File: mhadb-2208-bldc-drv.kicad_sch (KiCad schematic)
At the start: 60 parts, among them J1 TC2030, J2 Conn_01x04_Pin, J3 Conn_01x04, M2 Motor_3_Phases, SW1 SW_Push, SW4 SW_Push, U1 AS5600-ASOT, U10 DRV8311H, U2 SN65HVD230, U3 STM32F103C8Tx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

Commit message: schem/pcb: add motor mounting holes
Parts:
- added H1, H2, H3: MountingHole_Pad, GLCS:MountingHole_3.2mm_M3_DIN965_Pad_Thin, symbol Mechanical:MountingHole_Pad
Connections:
- net EPAD: now also H1.1, H2.1, H3.1
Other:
- note added: "Motor mounting"

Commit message: schem/pcb: fix DRV8311 nsleep
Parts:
- removed C42: 100u, Capacitor_SMD:CP_Elec_6.3x7.7, symbol Device:C_Polarized
- added C16, C17, C18: 22u, Capacitor_SMD:C_1206_3216Metric, symbol Device:C
- added R7: 10k, Resistor_SMD:R_0402_1005Metric, symbol Device:R
- added R8: 5k1, Resistor_SMD:R_0402_1005Metric, symbol Device:R
- J3: footprint Connector_JST:JST_PH_S4B-PH-K_1x04_P2.00mm_Horizontal -> Connector_JST:JST_XH_B4B-XH-A_1x04_P2.50mm_Vertical; JLCPCB Part # C157926 -> C144395; Manufacturer Part Number S4B-PH-K-S(LF)(SN) -> B4B-XH-A(LF)(SN)
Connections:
- net +BATT: now also C16.1, C17.1, C18.1, R7.2
- net EPAD: now also U3.20 (PB2), C16.2, C17.2, C18.2, R8.2
- net +5V: no longer names the net of U10.24 (~{SLEEP})
- net +5V: now also R7.1, R8.1
- no-connect marks 18 -> 17
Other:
- moved on the sheet: C39

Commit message: pcb: initial rough placement
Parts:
- removed TP3, TP8, TP9: TestPoint, TestPoint:TestPoint_Pad_D2.0mm, symbol Connector:TestPoint
- M2: footprint Connector_PinHeader_2.54mm:PinHeader_1x03_P2.54mm_Vertical -> GLCS:Connector_Pad_1x03
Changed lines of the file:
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@@
 	)
 	(junction
-		(at 227.33 116.84)
-		(diameter 0)
-		(color 0 0 0 0)
-	)
-	(junction
 		(at 214.63 139.7)
 		(diameter 0)
@@
 	)
 	(junction
-		(at 233.68 99.06)
-		(diameter 0)
-		(color 0 0 0 0)
-	)
-	(junction
 		(at 217.17 99.06)
 		(diameter 0)
@@
 	(wire
 		(pts
-			(xy 222.25 116.84) (xy 227.33 116.84)
+			(xy 222.25 116.84) (xy 228.6 116.84)
 		)
 		(stroke
@@
 	(wire
 		(pts
-			(xy 229.87 99.06) (xy 233.68 99.06)
+			(xy 229.87 99.06) (xy 237.49 99.06)
 		)
 		(stroke
@@
 	(wire
 		(pts
-			(xy 227.33 116.84) (xy 228.6 116.84)
-		)
-		(stroke
-			(width 0)
-			(type default)
-		)
-	)
-	(wire
-		(pts
 			(xy 259.08 93.98) (xy 264.16 93.98)
 		)
@@
 	(wire
 		(pts
-			(xy 233.68 99.06) (xy 237.49 99.06)
-		)
-		(stroke
-			(width 0)
-			(type default)
-		)
-	)
-	(wire
-		(pts
 			(xy 217.17 99.06) (xy 218.44 99.06)
 		)
@@
 	)
 	(symbol
-		(lib_id "Connector:TestPoint")
-		(at 233.68 99.06 0)
-		(unit 1)
-		(exclude_from_sim no)
-		(in_bom no)
-		(on_board yes)
-		(dnp no)
-		(fields_autoplaced yes)
-		(property "Reference" "TP9"
-			(at 236.22 95.7579 0)
-			(effects
-				(font
-					(size 1.27 1.27)
-				)
-				(justify left)
-			)
-		)
-		(property "Value" "TestPoint"
-			(at 236.22 97.0279 0)
-			(effects
-				(font
-					(size 1.27 1.27)
-				)
-				(justify left)
-				(hide yes)
-			)
-		)
-		(property "Footprint" "TestPoint:TestPoint_Pad_D2.0mm"
-			(at 238.76 99.06 0)
-			(effects
-				(font
-					(size 1.27 1.27)
-				)
-				(hide yes)
-			)
-		)
-		(property "Datasheet" "~"
-			(at 238.76 99.06 0)
-			(effects
-				(font
-					(size 1.27 1.27)
-				)
-				(hide yes)
-			)
-		)
-		(property "Description" "test point"
-			(at 233.68 99.06 0)
-			(effects
-				(font
-					(size 1.27 1.27)
-				)
-				(hide yes)
-			)
-		)
-		(pin "1"
-		)
-		(instances
-			(project "mhadb-2208-bldc-drv"
-				(path "/68a41d17-d2bf-47b9-9455-3cb873e40984"
-					(reference "TP9")
-					(unit 1)
-				)
-			)
-		)
-	)
-	(symbol
 		(lib_id "power:GND")
 		(at 91.44 63.5 0)
@@
 			)
 		)
-		(property "Footprint" "Connector_PinHeader_2.54mm:PinHeader_1x03_P2.54mm_Vertical"
+		(property "Footprint" "GLCS:Connector_Pad_1x03"
 			(at 266.7 135.636 0)
 			(effects
@@
 	)
 	(symbol
-		(lib_id "Connector:TestPoint")
-		(at 227.33 116.84 0)
-		(unit 1)
-		(exclude_from_sim no)
-		(in_bom no)
-		(on_board yes)
-		(dnp no)
-		(property "Reference" "TP8"
-			(at 228.854 112.268 0)
-			(effects
-				(font
-					(size 1.27 1.27)
-				)
-				(justify left)
-			)
-		)
-		(property "Value" "TestPoint"
-			(at 229.87 114.8079 0)
-			(effects
-				(font
-					(size 1.27 1.27)
-				)
-				(justify left)
-				(hide yes)
-			)
-		)
-		(property "Footprint" "TestPoint:TestPoint_Pad_D2.0mm"
-			(at 232.41 116.84 0)
-			(effects
-				(font
-					(size 1.27 1.27)
-				)
-				(hide yes)
-			)
-		)
-		(property "Datasheet" "~"
-			(at 232.41 116.84 0)
-			(effects
-				(font
-					(size 1.27 1.27)
-				)
-				(hide yes)
-			)
-		)
-		(property "Description" "test point"
-			(at 227.33 116.84 0)
-			(effects
-				(font
-					(size 1.27 1.27)
-				)
-				(hide yes)
-			)
-		)
-		(pin "1"
-		)
-		(instances
-			(project "mhadb-2208-bldc-drv"
-				(path "/68a41d17-d2bf-47b9-9455-3cb873e40984"
-					(reference "TP8")
-					(unit 1)
-				)
-			)
-		)
-	)
-	(symbol
 		(lib_id "power:GND")
 		(at 257.81 151.13 0)
@@
 					(unit 1)
 				)
-			)
-		)
-	)
-	(symbol
-		(lib_id "Connector:TestPoint")
-		(at 222.25 147.32 90)
-		(unit 1)
-		(exclude_from_sim no)
-		(in_bom no)
-		(on_board yes)
-		(dnp no)
-		(property "Reference" "TP3"
-			(at 220.472 145.288 90)
-			(effects
-				(font
-					(size 1.27 1.27)
-				)
-				(justify left)
-			)
-		)
-		(property "Value" "TestPoint"
-			(at 220.2179 144.78 0)
-			(effects
-				(font
-					(size 1.27 1.27)
-				)
-				(justify left)
-				(hide yes)
-			)
-		)
-		(property "Footprint" "TestPoint:TestPoint_Pad_D2.0mm"
-			(at 222.25 142.24 0)
-			(effects
-				(font
-					(size 1.27 1.27)
-				)
-				(hide yes)
-			)
-		)
-		(property "Datasheet" "~"
-			(at 222.25 142.24 0)
-			(effects
-				(font
-					(size 1.27 1.27)
-				)
-				(hide yes)
-			)
-		)
-		(property "Description" "test point"
-			(at 222.25 147.32 0)
-			(effects
-				(font
-					(size 1.27 1.27)
-				)
-				(hide yes)
-			)
-		)
-		(pin "1"
-		)
-		(instances
-			(project "mhadb-2208-bldc-drv"
-				(path "/68a41d17-d2bf-47b9-9455-3cb873e40984"
-					(reference "TP3")
-					(unit 1)
-				)

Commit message: pcb: initial components placement
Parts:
- removed TP6: TestPoint, TestPoint:TestPoint_Pad_D2.0mm, symbol Connector:TestPoint
- added C19: 0u1, Capacitor_SMD:C_0402_1005Metric, symbol Device:C
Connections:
- net +3V3: now also C19.1
- net EPAD: now also C19.2
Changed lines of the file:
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@@
 	)
 	(junction
-		(at 254 74.93)
-		(diameter 0)
-		(color 0 0 0 0)
-	)
-	(junction
 		(at 91.44 52.07)
 		(diameter 0)
@@
 	)
 	(junction
-		(at 152.4 60.96)
-		(diameter 0)
-		(color 0 0 0 0)
-	)
-	(junction
 		(at 123.19 62.23)
 		(diameter 0)
@@
 	(wire
 		(pts
-			(xy 152.4 57.15) (xy 152.4 60.96)
+			(xy 152.4 57.15) (xy 152.4 64.77)
 		)
 		(stroke
@@
 	(wire
 		(pts
-			(xy 152.4 60.96) (xy 152.4 64.77)
-		)
-		(stroke
-			(width 0)
-			(type default)
-		)
-	)
-	(wire
-		(pts
 			(xy 81.28 181.61) (xy 81.28 182.88)
 		)
@@
 	(wire
 		(pts
-			(xy 255.27 74.93) (xy 254 74.93)
-		)
-		(stroke
-			(width 0)
-			(type default)
-		)
-	)
-	(wire
-		(pts
 			(xy 139.7 64.77) (xy 139.7 66.04)
 		)
@@
 	)
 	(symbol
-		(lib_id "Connector:TestPoint")
-		(at 152.4 60.96 90)
+		(lib_id "Device:C")
+		(at 102.87 57.15 0)
 		(unit 1)
 		(exclude_from_sim no)
-		(in_bom no)
+		(in_bom yes)
 		(on_board yes)
 		(dnp no)
-		(fields_autoplaced yes)
-		(property "Reference" "TP6"
-			(at 149.098 58.42 90)
+		(property "Reference" "C19"
+			(at 105.664 55.88 0)
 			(effects
 				(font
 					(size 1.27 1.27)
 				)
+				(justify left)
 			)
 		)
-		(property "Value" "TestPoint"
-			(at 150.3679 58.42 0)
+		(property "Value" "0u1"
+			(at 105.664 58.42 0)
 			(effects
 				(font
@@
 				)
 				(justify left)
-				(hide yes)
 			)
 		)
-		(property "Footprint" "TestPoint:TestPoint_Pad_D2.0mm"
-			(at 152.4 55.88 0)
+		(property "Footprint" "Capacitor_SMD:C_0402_1005Metric"
+			(at 103.8352 60.96 0)
 			(effects
 				(font
@@
 		)
 		(property "Datasheet" "~"
-			(at 152.4 55.88 0)
+			(at 102.87 57.15 0)
 			(effects
 				(font
@@
 			)
 		)
-		(property "Description" "test point"
-			(at 152.4 60.96 0)
+		(property "Description" "Unpolarized capacitor"
+			(at 102.87 57.15 0)
+			(effects
+				(font
+					(size 1.27 1.27)
+				)
+				(hide yes)
+			)
+		)
+		(property "Basic" "Y"
+			(at 102.87 57.15 0)
 			(effects
 				(font
@@
 			)
 		)
+		(property "JLCPCB Part #" "C307331"
+			(at 102.87 57.15 0)
+			(effects
+				(font
+					(size 1.27 1.27)
+				)
+				(hide yes)
+			)
+		)
+		(property "Manufacturer" "Samsung Electro-Mechanics "
+			(at 102.87 57.15 0)
+			(effects
+				(font
+					(size 1.27 1.27)
+				)
+				(hide yes)
+			)
+		)
+		(property "Manufacturer Part Number" "CL05B104KB54PNC"
+			(at 102.87 57.15 0)
+			(effects
+				(font
+					(size 1.27 1.27)
+				)
+				(hide yes)
+			)
+		)
+		(pin "2"
+		)
 		(pin "1"
 		)
@@
 			(project "mhadb-2208-bldc-drv"
 				(path "/68a41d17-d2bf-47b9-9455-3cb873e40984"
-					(reference "TP6")
+					(reference "C19")
 					(unit 1)
 				)

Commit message: schem: set DNP on wrongly rated tvs diode
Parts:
- D8: now not fitted
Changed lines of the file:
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@@
 		(in_bom yes)
 		(on_board yes)
-		(dnp no)
+		(dnp yes)
 		(property "Reference" "D8"
 			(at 88.646 183.896 90)

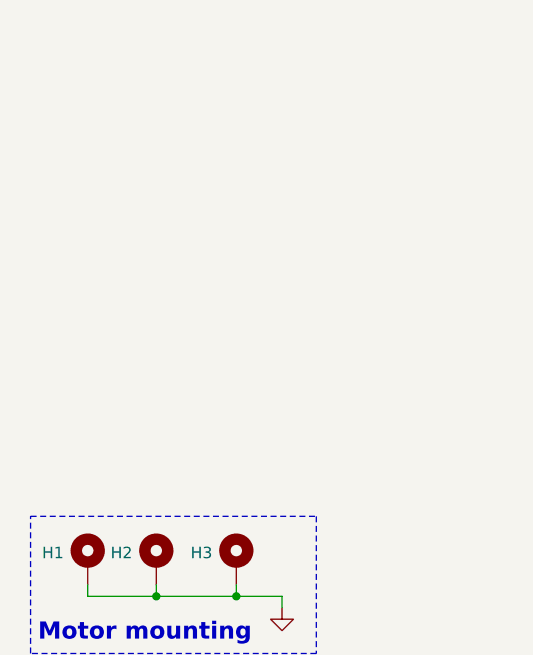
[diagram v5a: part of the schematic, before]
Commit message: schem: add power led indicators
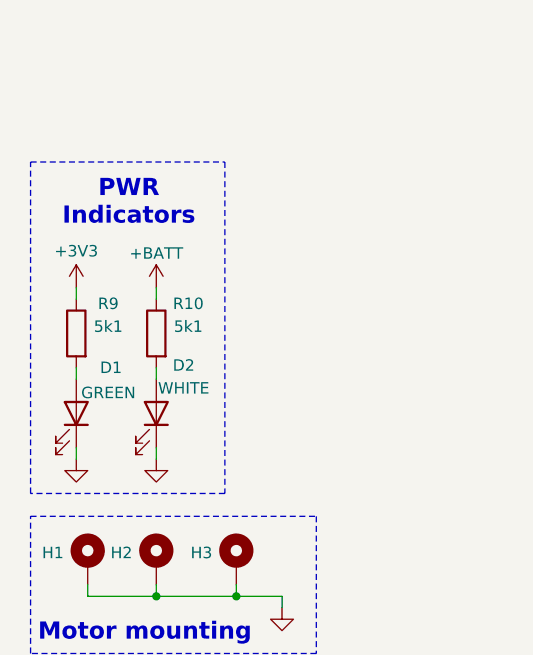
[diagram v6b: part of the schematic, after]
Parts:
- added D1: GREEN, LED_SMD:LED_0805_2012Metric, symbol Device:LED
- added D2: WHITE, LED_SMD:LED_0603_1608Metric, symbol Device:LED
- added R10, R9: 5k1, Resistor_SMD:R_0402_1005Metric, symbol Device:R
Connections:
- net +3V3: now also R9.1
- net +BATT: now also R10.1
- net EPAD: now also D1.1 (K), D2.1 (K)
- new net: D1.2 (A), R9.2
- new net: D2.2 (A), R10.2
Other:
- note added: "PWR Indicators"

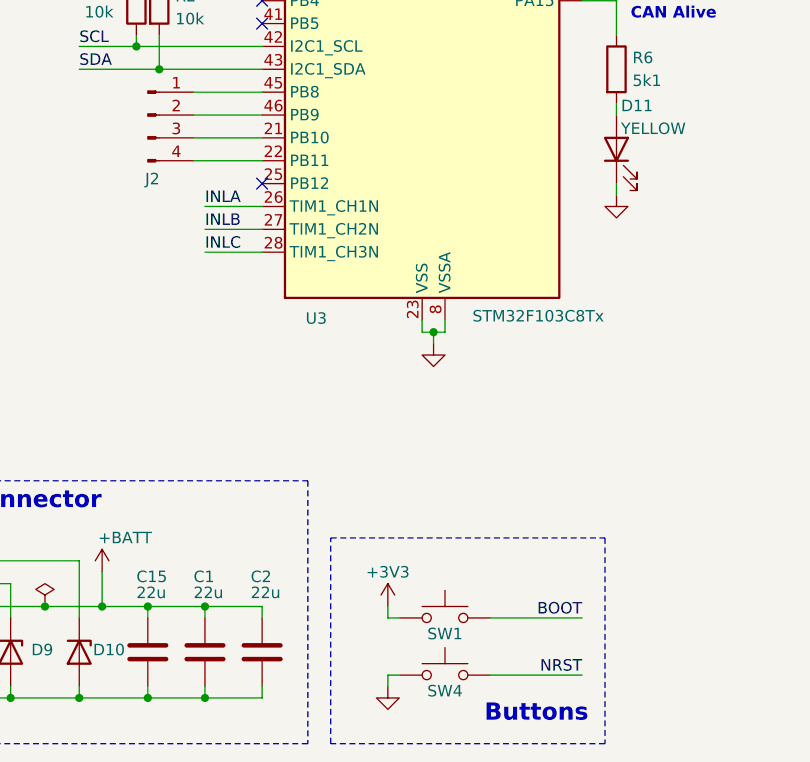
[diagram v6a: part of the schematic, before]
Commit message: schem: add BTN
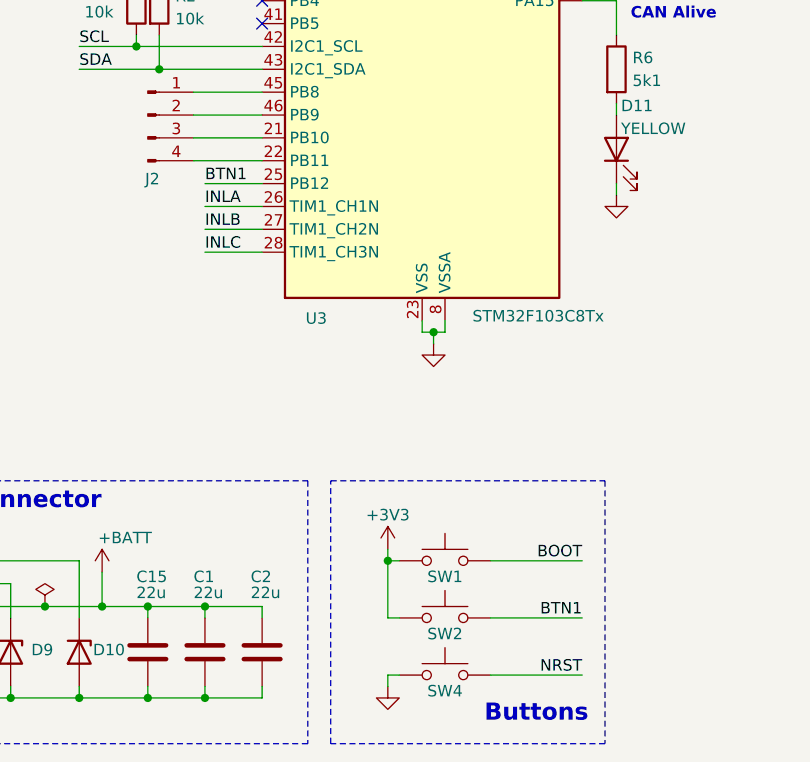
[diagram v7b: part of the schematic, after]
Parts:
- added SW2: SW_Push, Button_Switch_SMD:SW_SPST_TS-1088-xR020, symbol Switch:SW_Push
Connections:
- net +3V3: now also SW2.1
- net BTN1: now reaches U3.25 (PB12)
- net BTN1: now also SW2.2
- no-connect marks 17 -> 16
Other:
- moved on the sheet: SW1
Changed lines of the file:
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@@
 	)
 	(rectangle
-		(start 129.54 171.45)
+		(start 129.54 165.1)
 		(end 160.02 194.31)
 		(stroke
@@
 	)
 	(junction
+		(at 135.89 173.99)
+		(diameter 0)
+		(color 0 0 0 0)
+	)
+	(junction
 		(at 217.17 99.06)
 		(diameter 0)
@@
 	)
 	(no_connect
-		(at 121.92 132.08)
-	)
-	(no_connect
 		(at 273.05 74.93)
 	)
@@
 	(wire
 		(pts
+			(xy 137.16 180.34) (xy 135.89 180.34)
+		)
+		(stroke
+			(width 0)
+			(type default)
+		)
+	)
+	(wire
+		(pts
 			(xy 140.97 148.59) (xy 139.7 148.59)
 		)
@@
 	(wire
 		(pts
-			(xy 137.16 180.34) (xy 135.89 180.34)
+			(xy 137.16 173.99) (xy 135.89 173.99)
 		)
 		(stroke
@@
 	(wire
 		(pts
+			(xy 135.89 173.99) (xy 135.89 180.34)
+		)
+		(stroke
+			(width 0)
+			(type default)
+		)
+	)
+	(wire
+		(pts
 			(xy 264.16 104.14) (xy 264.16 102.87)
 		)
@@
 	(wire
 		(pts
-			(xy 147.32 180.34) (xy 157.48 180.34)
+			(xy 147.32 173.99) (xy 157.48 173.99)
 		)
 		(stroke
@@
 	(wire
 		(pts
-			(xy 135.89 180.34) (xy 135.89 179.07)
+			(xy 135.89 173.99) (xy 135.89 172.72)
 		)
 		(stroke
@@
 	(wire
 		(pts
+			(xy 147.32 180.34) (xy 157.48 180.34)
+		)
+		(stroke
+			(width 0)
+			(type default)
+		)
+	)
+	(wire
+		(pts
 			(xy 135.89 186.69) (xy 137.16 186.69)
 		)
@@
 	(wire
 		(pts
+			(xy 115.57 132.08) (xy 121.92 132.08)
+		)
+		(stroke
+			(width 0)
+			(type default)
+		)
+	)
+	(wire
+		(pts
 			(xy 224.79 109.22) (xy 224.79 107.95)
 		)
@@
 	)
 	(label "BOOT"
-		(at 157.48 180.34 180)
+		(at 157.48 173.99 180)
 		(effects
 			(font
@@
 		)
 	)
+	(label "BTN1"
+		(at 157.48 180.34 180)
+		(effects
+			(font
+				(size 1.27 1.27)
+			)
+			(justify right bottom)
+		)
+	)
 	(label "SDA"
 		(at 278.13 67.31 180)
@@
 		)
 	)
+	(label "BTN1"
+		(at 115.57 132.08 0)
+		(effects
+			(font
+				(size 1.27 1.27)
+			)
+			(justify left bottom)
+		)
+	)
 	(label "BOOT"
 		(at 110.49 78.74 0)
@@
 	(symbol
 		(lib_id "Switch:SW_Push")
-		(at 142.24 180.34 0)
+		(at 142.24 173.99 0)
 		(unit 1)
 		(exclude_from_sim no)
@@
 		(dnp no)
 		(property "Reference" "SW1"
-			(at 142.24 182.118 0)
+			(at 142.24 175.768 0)
 			(effects
 				(font
@@
 		)
 		(property "Value" "SW_Push"
-			(at 142.24 175.26 0)
+			(at 142.24 168.91 0)
 			(effects
 				(font
@@
 		)
 		(property "Footprint" "Button_Switch_SMD:SW_SPST_TS-1088-xR020"
-			(at 142.24 175.26 0)
+			(at 142.24 168.91 0)
 			(effects
 				(font
@@
 		)
 		(property "Datasheet" "~"
-			(at 142.24 175.26 0)
+			(at 142.24 168.91 0)
 			(effects
 				(font
@@
 		)
 		(property "Description" "Push button switch, generic, two pins"
-			(at 142.24 180.34 0)
+			(at 142.24 173.99 0)
 			(effects
 				(font
@@
 		)
 		(property "Manufacturer" "XUNPU"
-			(at 142.24 180.34 0)
+			(at 142.24 173.99 0)
 			(effects
 				(font
@@
 		)
 		(property "Manufacturer Part Number" "TS-1088-AR02016"
-			(at 142.24 180.34 0)
+			(at 142.24 173.99 0)
 			(effects
 				(font
@@
 		)
 		(property "Basic" "Y"
-			(at 142.24 180.34 0)
+			(at 142.24 173.99 0)
 			(effects
 				(font
@@
 		)
 		(property "JLCPCB Part #" "C720477"
-			(at 142.24 180.34 0)
+			(at 142.24 173.99 0)
 			(effects
 				(font
@@
 	(symbol
 		(lib_id "power:+3V3")
-		(at 135.89 179.07 0)
+		(at 135.89 172.72 0)
 		(unit 1)
 		(exclude_from_sim no)
@@
 		(dnp no)
 		(property "Reference" "#PWR020"
-			(at 135.89 182.88 0)
+			(at 135.89 176.53 0)
 			(effects
 				(font
@@
 		)
 		(property "Value" "+3V3"
-			(at 135.89 175.26 0)
+			(at 135.89 168.91 0)
 			(effects
 				(font
@@
 		)
 		(property "Footprint" ""
-			(at 135.89 179.07 0)
+			(at 135.89 172.72 0)
 			(effects
 				(font
@@
 		)
 		(property "Datasheet" ""
-			(at 135.89 179.07 0)
+			(at 135.89 172.72 0)
 			(effects
 				(font
@@
 		)
 		(property "Description" "Power symbol creates a global label with name \"+3V3\""
-			(at 135.89 179.07 0)
+			(at 135.89 172.72 0)
 			(effects
 				(font
@@
 					(unit 1)
 				)
+			)
+		)
+	)
+	(symbol
+		(lib_id "Switch:SW_Push")
+		(at 142.24 180.34 0)
+		(unit 1)
+		(exclude_from_sim no)
+		(in_bom yes)
+		(on_board yes)
+		(dnp no)
+		(property "Reference" "SW2"
+			(at 142.24 182.118 0)
+			(effects
+				(font
+					(size 1.27 1.27)
+				)
+			)
+		)
+		(property "Value" "SW_Push"
+			(at 142.24 175.26 0)
+			(effects
+				(font
+					(size 1.27 1.27)
+				)
+				(hide yes)
+			)
+		)
+		(property "Footprint" "Button_Switch_SMD:SW_SPST_TS-1088-xR020"
+			(at 142.24 175.26 0)
+			(effects
+				(font
+					(size 1.27 1.27)
+				)
+				(hide yes)
+			)
+		)
+		(property "Datasheet" "~"
+			(at 142.24 175.26 0)
+			(effects
+				(font
+					(size 1.27 1.27)
+				)
+				(hide yes)
+			)
+		)
+		(property "Description" "Push button switch, generic, two pins"
+			(at 142.24 180.34 0)
+			(effects
+				(font
+					(size 1.27 1.27)
+				)
+				(hide yes)
+			)
+		)
+		(property "Manufacturer" "XUNPU"
+			(at 142.24 180.34 0)
+			(effects
+				(font
+					(size 1.27 1.27)
+				)
+				(hide yes)
+			)
+		)
+		(property "Manufacturer Part Number" "TS-1088-AR02016"
+			(at 142.24 180.34 0)
+			(effects
+				(font
+					(size 1.27 1.27)
+				)
+				(hide yes)
+			)
+		)
+		(property "Basic" "Y"
+			(at 142.24 180.34 0)
+			(effects
+				(font
+					(size 1.27 1.27)
+				)
+				(hide yes)
+			)
+		)
+		(property "JLCPCB Part #" "C720477"
+			(at 142.24 180.34 0)
+			(effects
+				(font
+					(size 1.27 1.27)
+				)
+				(hide yes)
+			)
+		)
+		(pin "2"
+		)
+		(pin "1"
+		)
+		(instances
+			(project "mhadb-2208-bldc-drv"
+				(path "/68a41d17-d2bf-47b9-9455-3cb873e40984"
+					(reference "SW2")
+					(unit 1)
+				)

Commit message: schem: add missing info to BOM
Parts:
- U1: Basic (none) -> X; JLCPCB Part # (none) -> C499458; Manufacturer (none) -> AMS; Manufacturer Part Number (none) -> AS5600-ASOT
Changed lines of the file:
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@@
+			)
+		)
+		(property "Basic" "X"
+			(at 256.54 62.23 0)
+			(effects
+				(font
+					(size 1.27 1.27)
+				)
+				(hide yes)
+			)
+		)
+		(property "JLCPCB Part #" "C499458"
+			(at 256.54 62.23 0)
+			(effects
+				(font
+					(size 1.27 1.27)
+				)
+				(hide yes)
+			)
+		)
+		(property "Manufacturer" "AMS"
+			(at 256.54 62.23 0)
+			(effects
+				(font
+					(size 1.27 1.27)
+				)
+				(hide yes)
+			)
+		)
+		(property "Manufacturer Part Number" "AS5600-ASOT"
+			(at 256.54 62.23 0)
+			(effects
+				(font
+					(size 1.27 1.27)
+				)
+				(hide yes)
 			)
 		)
